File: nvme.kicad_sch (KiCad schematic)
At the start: 12 parts, among them J3 pcie_m2_ngff, U19 ISL91127IRNZ

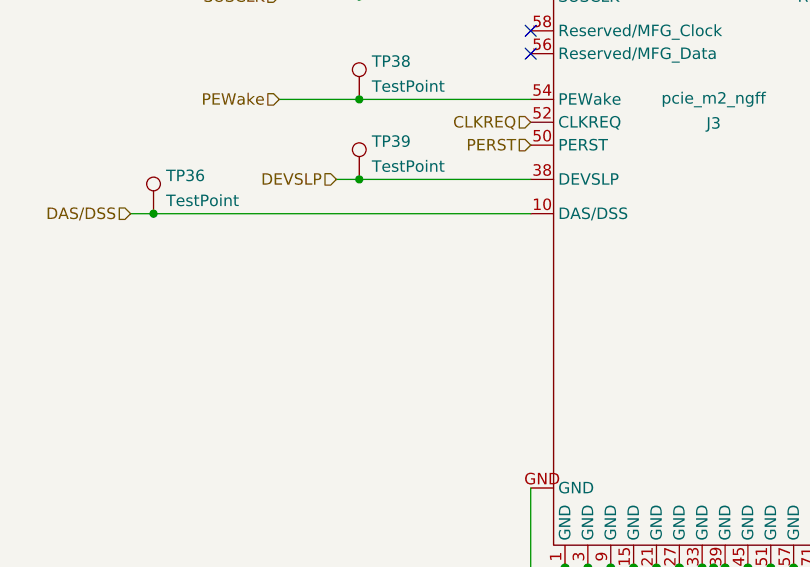
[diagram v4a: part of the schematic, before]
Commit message: Add a bunch more 3d models
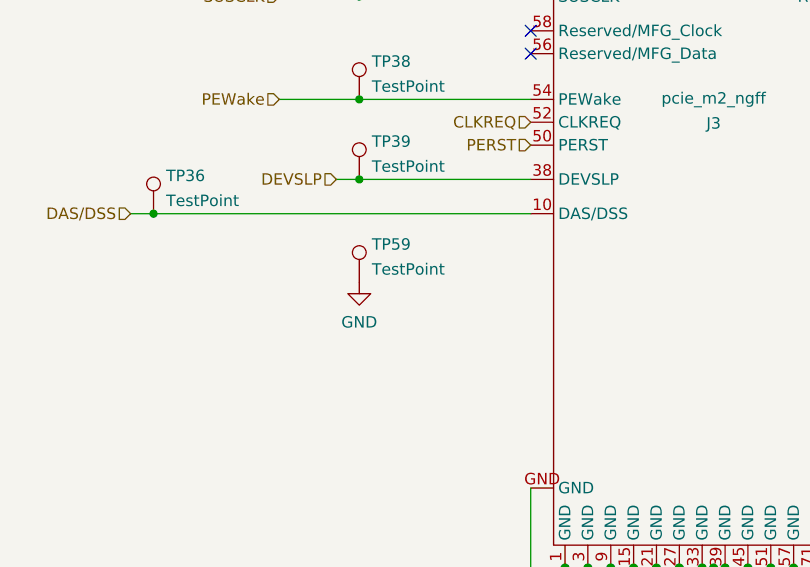
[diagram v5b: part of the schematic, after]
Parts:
- added TP59: TestPoint, footprints:testpoint_small, symbol Connector:TestPoint
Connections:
- net GND: now also TP59.1
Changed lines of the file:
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@@
     (pin "2")
+  )
+  (symbol (lib_id "Connector:TestPoint") (at 179.07 106.68 0) (unit 1)
+    (in_bom yes) (on_board yes) (fields_autoplaced)
+    (property "Reference" "TP59" (id 0) (at 180.467 102.4695 0)
+      (effects (font (size 1.27 1.27)) (justify left))
+    )
+    (property "Value" "TestPoint" (id 1) (at 180.467 105.2446 0)
+      (effects (font (size 1.27 1.27)) (justify left))
+    )
+    (property "Footprint" "footprints:testpoint_small" (id 2) (at 184.15 106.68 0)
+      (effects (font (size 1.27 1.27)) hide)
+    )
+    (property "Datasheet" "~" (id 3) (at 184.15 106.68 0)
+      (effects (font (size 1.27 1.27)) hide)
+    )
+    (pin "1")
   )
   (symbol (lib_id "Connector:TestPoint") (at 254 68.58 0) (unit 1)
@@
     (pin "2")
   )
+  (symbol (lib_id "power:GND") (at 179.07 106.68 0) (unit 1)
+    (in_bom yes) (on_board yes) (fields_autoplaced)
+    (property "Reference" "#PWR029" (id 0) (at 179.07 113.03 0)
+      (effects (font (size 1.27 1.27)) hide)
+    )
+    (property "Value" "GND" (id 1) (at 179.07 111.1234 0))
+    (property "Footprint" "" (id 2) (at 179.07 106.68 0)
+      (effects (font (size 1.27 1.27)) hide)
+    )
+    (property "Datasheet" "" (id 3) (at 179.07 106.68 0)
+      (effects (font (size 1.27 1.27)) hide)
+    )
+    (pin "1")
+  )
 )

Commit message: Board rev2 ready to order, hopefully
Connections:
- net RX_N: now also J3.41 (PETn0); no longer J3.47 (PERn0)
- net RX_P: now also J3.43 (PETp0); no longer J3.49 (PERp0)
- net TX_N: now also J3.47 (PERn0); no longer J3.41 (PETn0)
- net TX_P: now also J3.49 (PERp0); no longer J3.43 (PETp0)
